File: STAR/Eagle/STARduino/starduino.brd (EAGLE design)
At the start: 101.6 x 38.1 mm, 80 parts, among them J3 J30J-15J30, J4 J30J-31J30, Q2 BSS8402DW, Q3 BSS8402DW, U1 SSCMNNN015PA2A3, U10 MC14504BDTG, U11 MAX31725MTA+, U12 TCA9535_RTW_24, U13 BMX055, U15 MC74VHC1GT125, U16 PCA9515A, U17 PCA9306DCT, U18 LT8616, U4 DS3231MZ+, U6 ATSAMD21G18, U8 ADXL375BCCZ

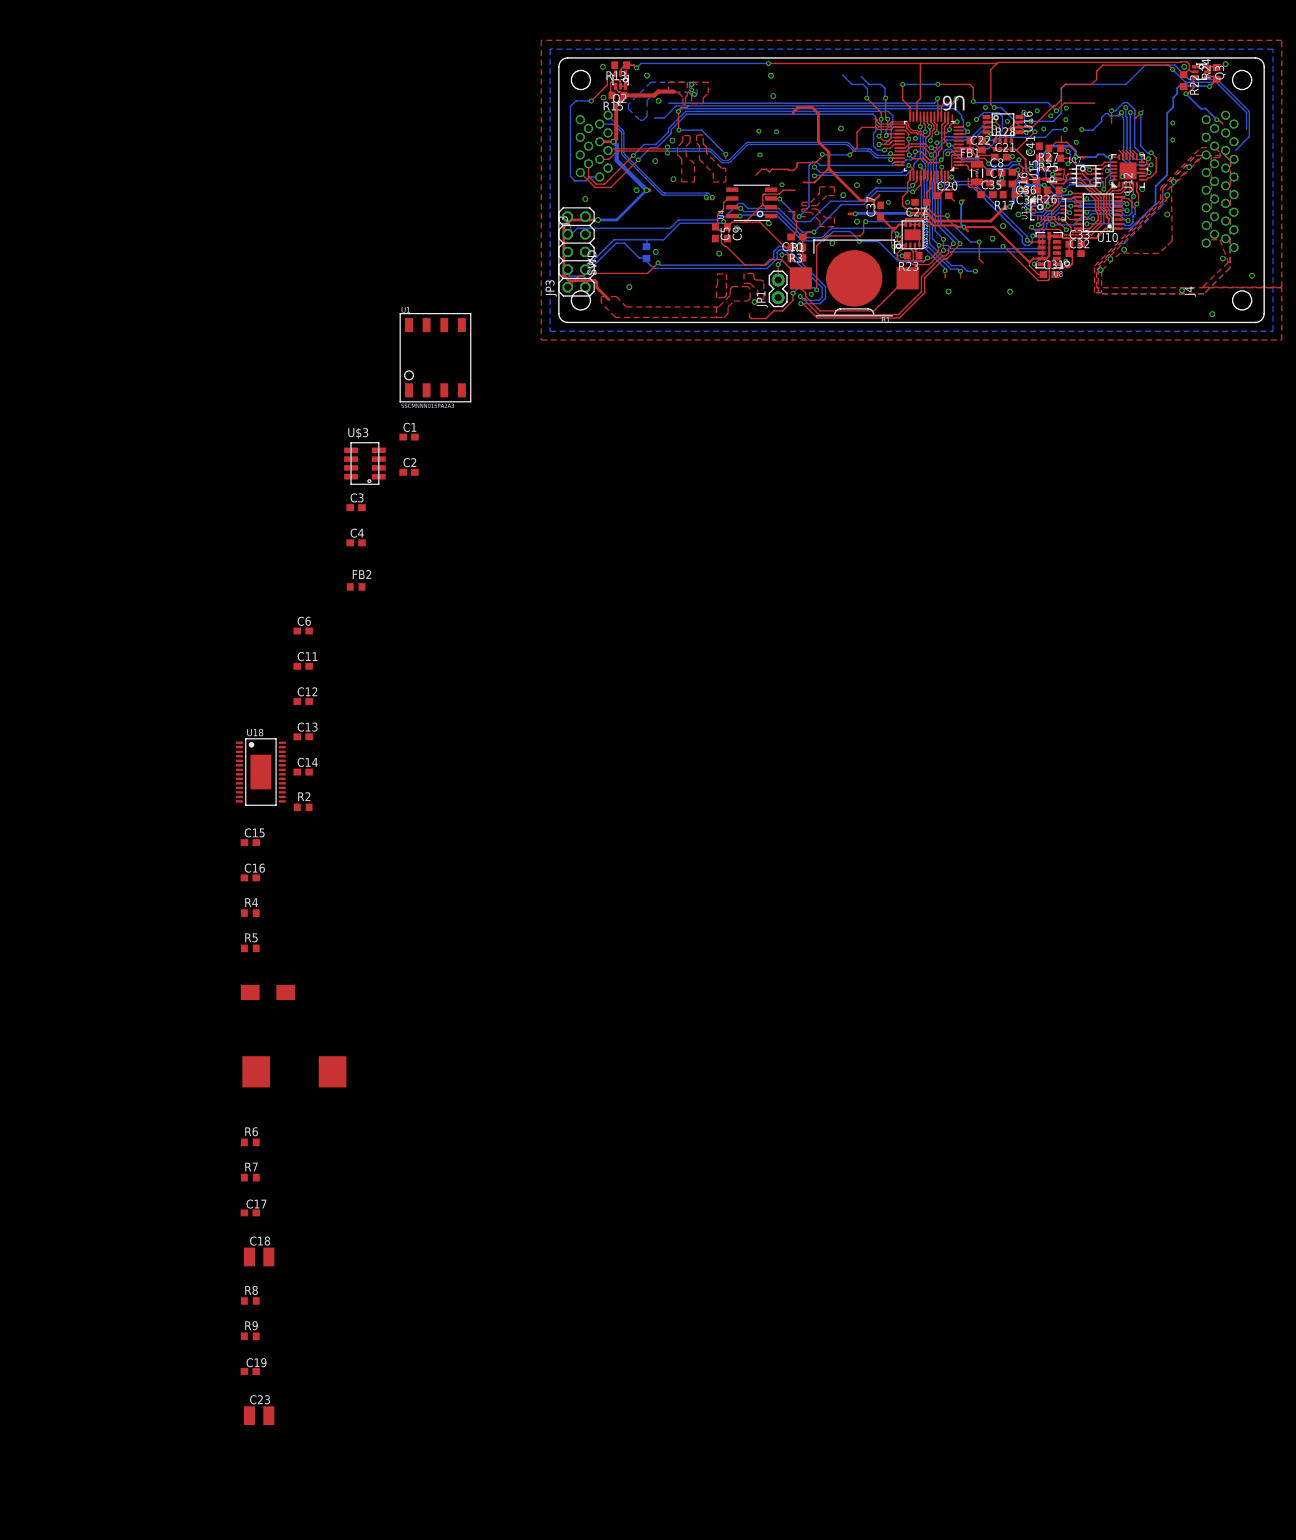
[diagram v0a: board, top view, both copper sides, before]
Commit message: datalogger differential pairs
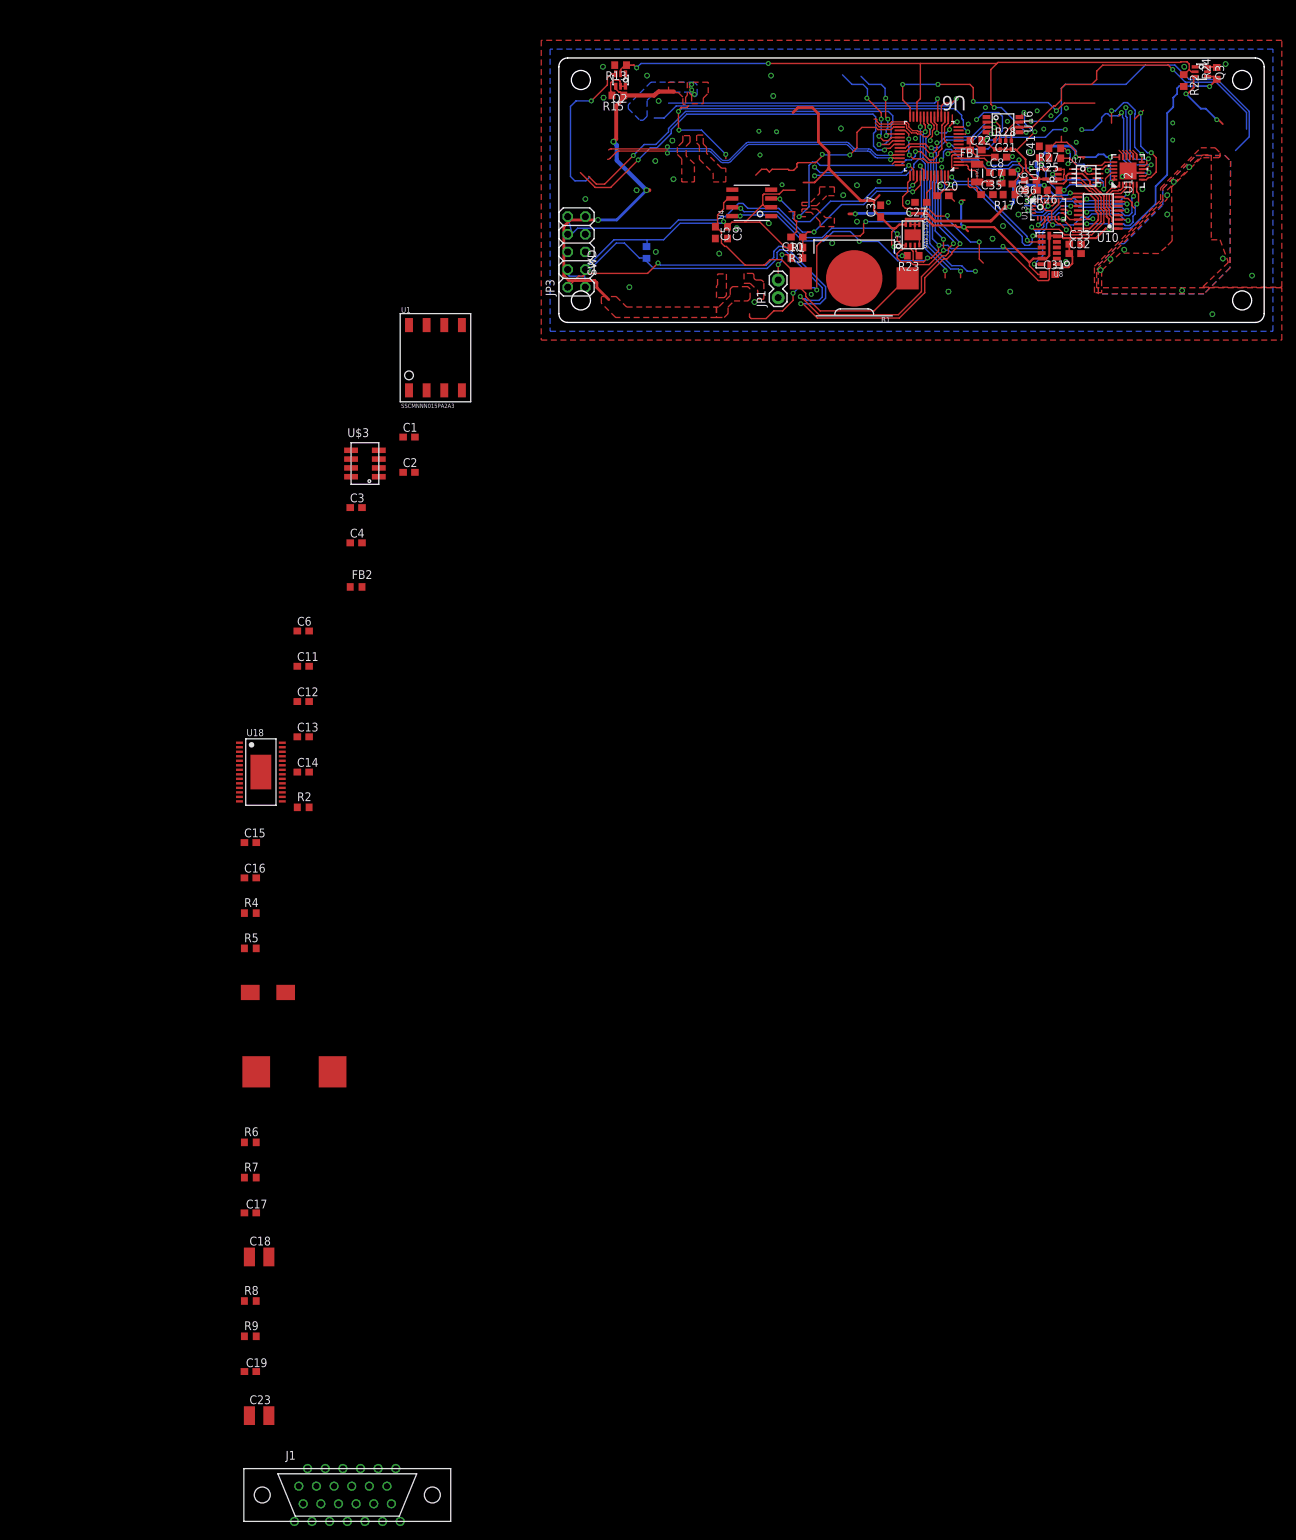
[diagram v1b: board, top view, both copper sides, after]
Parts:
- removed J3: J30J-15J30, CM_J30J:ZKN-15-J30
- removed J4: J30J-31J30, CM_J30J:ZKN-31-J30
- added J1: J30J-25, CM_J30J:ZKN-25
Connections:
- removed net PI_D_N: J3.7
- removed net PI_D_P: J3.8
- new net BIAS_REF: J1.2, U6.7
- new net D: J1.10
- new net N$27: J1.11
- new net N$32: J1.12
- new net N$36: J1.13
- new net SD_STAR: J1.9
- net +3V3: now also J1.14
- net +5V: now also J1.15, J1.16, J1.17, J1.18, J1.19; no longer J3.5
- net DEBUG_5V: no longer J3.1
- net GND: now also J1.20, J1.21, J1.22, J1.23, J1.24, J1.25; no longer J3.14, J3.2, J3.6
- net MISO: now also J1.3, J1.4
- net MOSI: now also J1.5, J1.6
- net RX2: no longer J3.9
- net SCK: now also J1.7, J1.8
- net TX2: no longer J3.10
- net USB_D_N: no longer J3.4
- net USB_D_P: no longer J3.3
- net VDD: now also J1.1
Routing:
- net PI_D_N: track 22.9 -> 0.00 mm, vias 1 -> 0
- net PI_D_P: track 22.8 -> 0.00 mm, vias 1 -> 0
- net +5V: track 57.4 -> 55.5 mm
- net TX2: track 59.6 -> 57.8 mm
- net DEBUG_5V: track 23.9 -> 22.4 mm
- net USB_D_P: track 47.0 -> 45.9 mm

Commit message: got rid of old STARduino routing
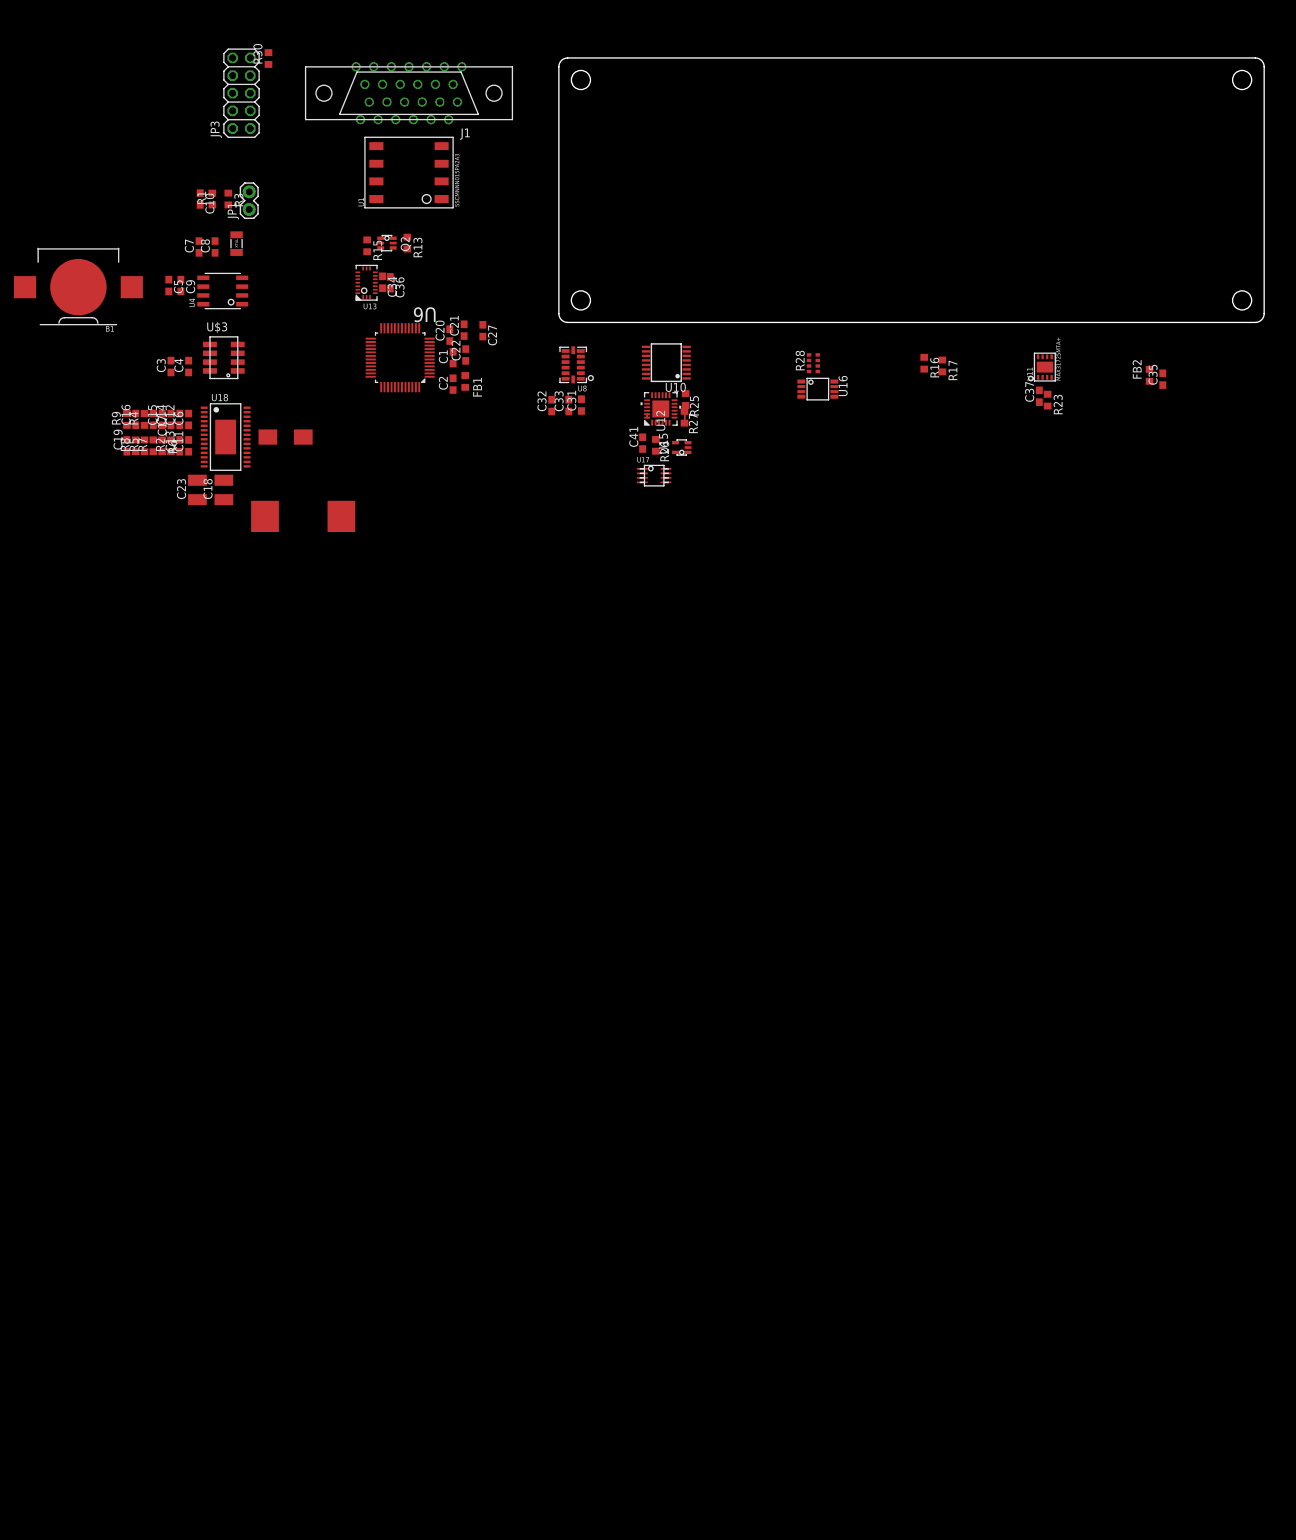
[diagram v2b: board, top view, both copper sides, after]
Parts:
- removed Q3: BSS8402DW, transistor-fet:SC70
- removed R22: 100k, resistor:R0603
- removed R24: 191k, resistor:R0603
- moved J1 202.1 mm to (-21.6, 33.0), turned to 180 degrees
- moved C19 134.5 mm to (-62.2, -17.8), turned to 90 degrees
- moved C23 133.6 mm to (-52.1, -24.1), turned to 90 degrees
- moved R9 133.3 mm to (-62.2, -14.0), turned to 90 degrees
- moved R8 124.3 mm to (-61.0, -17.8), turned to 90 degrees
- moved FB2 118.3 mm to (85.1, -7.62), turned to 90 degrees
- moved C17 115.2 mm to (-58.4, -14.0), turned to 270 degrees
- moved C7 115.1 mm to (-51.8, 10.9), turned to 90 degrees
- moved C8 113.0 mm to (-49.5, 10.9), turned to 90 degrees
- moved B1 111.8 mm to (-69.2, 5.08)
- moved C18 110.6 mm to (-48.3, -24.1), turned to 90 degrees
- moved XTAL1 107.2 mm to (-46.4, 11.4)
- moved R7 106.3 mm to (-58.4, -17.8), turned to 90 degrees
- moved R6 101.1 mm to (-57.1, -17.8), turned to 270 degrees
- moved U13 98.8 mm to (-27.7, 5.71), turned to 180 degrees
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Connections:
- removed net EXTERNAL_3V3: Q3.3
- removed net N$18: Q3.5, Q3.6, R24.2
- new net N$2: C4.2, U$3.P$5
- net +3V3: no longer Q3.4, R24.1
- net EXTERNAL_KILL: no longer Q3.2, R22.1
- net GND: no longer C4.2, Q3.1, R22.2, U$3.P$5
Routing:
- net +3V3: track 250.0 -> 0.00 mm, vias 15 -> 0
- net SCL: track 132.8 -> 0.00 mm, vias 10 -> 0
- net SDA: track 113.8 -> 0.00 mm, vias 8 -> 0
- net EXTERNAL_KILL: track 108.1 -> 0.00 mm, vias 4 -> 0
- net SWDIO: track 91.8 -> 0.00 mm, vias 4 -> 0
- net SWDCLK: track 91.0 -> 0.00 mm, vias 3 -> 0
- net 5V_S: track 85.4 -> 3.05 mm, vias 10 -> 0
- net RESET: track 65.5 -> 0.00 mm, vias 2 -> 0
- net I_SENSE: track 59.0 -> 0.00 mm, vias 4 -> 0
- net TX2: track 57.8 -> 0.00 mm, vias 2 -> 0
- net RX2: track 57.0 -> 0.00 mm, vias 2 -> 0
- net +5V: track 55.5 -> 0.00 mm, vias 3 -> 0
- net SCL_BUFF: track 51.7 -> 0.00 mm, vias 1 -> 0
- net TX0: track 48.9 -> 0.00 mm, vias 1 -> 0
- net SDA_BUFF: track 46.2 -> 0.00 mm, vias 1 -> 0
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- removed copper zone on layer 1, net +5V
- removed copper zone on layer 1, net 5V_S
- removed copper zone on layer 1, net GND
- removed copper zone on layer 16, net GND
- removed copper zone on layer 1, net N$15
- removed copper zone on layer 1, net N$39
- removed copper zone on layer 1, net N$40
- removed copper zone on layer 1, net N$50
- removed copper zone on layer 1, net N$51
- removed copper zone on layer 1, net VCC
- removed copper zone on layer 16, net VCC
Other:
- board text added: "STARduino"
- board text removed: "5-2017 Rev. 2"
- board text removed: "SWD"

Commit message: half a routed STARduino
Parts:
- moved B1 112.2 mm to (39.7, 32.1), turned to 0 degrees
- moved C23 98.1 mm to (39.1, 12.1), turned to 180 degrees
- moved R6 95.2 mm to (20.7, 37.0), turned to 180 degrees
- moved R7 94.0 mm to (18.5, 36.3)
- moved R4 93.8 mm to (20.6, 34.6), turned to 0 degrees
- moved C17 93.4 mm to (20.6, 35.8), turned to 180 degrees
- moved C16 92.6 mm to (21.0, 29.1), turned to 180 degrees
- moved R5 89.7 mm to (18.0, 27.0), turned to 180 degrees
- moved C15 89.7 mm to (19.9, 31.9)
- moved C13 87.0 mm to (18.5, 29.5), turned to 270 degrees
- moved C19 86.4 mm to (12.3, 26.0)
- moved C5 84.6 mm to (25.0, 29.2), turned to 180 degrees
- moved R8 83.0 mm to (9.53, 26.0)
- moved L1 82.8 mm to (26.1, 34.2)
- moved C11 81.5 mm to (7.75, 36.1), turned to 270 degrees
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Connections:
- removed net N$13: C15.2
- removed net N$16: C16.2
- net GND: now also C3.1
- net N$14: now also C15.2
- net N$17: now also C16.2
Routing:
- net +3V3: track 0.00 -> 194.8 mm, vias 0 -> 2
- net +5V: track 0.00 -> 89.4 mm, vias 0 -> 2
- net GND: track 0.00 -> 43.6 mm, vias 0 -> 5
- net N$8: track 0.00 -> 34.0 mm, vias 0 -> 2
- net RESET: track 0.00 -> 24.9 mm, vias 0 -> 2
- net VDD: track 0.00 -> 22.3 mm, vias 0 -> 2
- net N$37: track 0.00 -> 16.4 mm, vias 0 -> 2
- net N$1: track 0.00 -> 15.4 mm, vias 0 -> 2
- net SCL: track 0.00 -> 12.0 mm, vias 0 -> 2
- net SDA: track 0.00 -> 11.7 mm, vias 0 -> 2
- net N$21: track 0.00 -> 10.8 mm, vias 0 -> 2
- net N$11: track 0.00 -> 10.8 mm, vias 0 -> 2
- net SDA_BUFF: track 0.00 -> 10.7 mm
- net N$6: track 0.00 -> 10.6 mm, vias 0 -> 2
- net SCL_BUFF: track 0.00 -> 9.46 mm
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- added copper zone on layer 1, net GND
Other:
- board size 101.6 x 38.1 mm -> 59.8 x 38.2 mm

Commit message: STARduino
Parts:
- moved U$1 39.9 mm to (25.2, 12.1)
- moved U$2 39.9 mm to (12.3, 11.9)
- moved C27 2.53 mm to (21.4, 17.3), turned to 90 degrees
- moved XTAL1 2.12 mm to (22.7, 11.1)
- moved C7 1.82 mm to (25.3, 12.4), turned to 180 degrees
- moved C18 1.79 mm to (19.4, 11.0)
- moved C23 1.53 mm to (39.0, 10.6)
- moved U12 1.14 mm to (45.4, 23.0)
- moved C8 0.48 mm to (27.9, 9.45), turned to 270 degrees
- moved C41 0.32 mm to (47.7, 9.40)
- moved FB2 0.09 mm to (51.1, 2.22)
- moved C33 0.06 mm to (53.8, 2.24)
- moved C35 0.06 mm to (52.5, 2.24)
- moved C11 0.06 mm to (7.75, 36.2)
- moved C31 0.06 mm to (52.5, 5.30)
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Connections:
- net +3V3: now also J1.1, J1.3; no longer J1.14
- net +5V: now also J1.20, J1.5, J1.6, J1.8; no longer J1.15, J1.16, J1.17, J1.18
- net GND: now also J1.7; no longer J1.20, J1.25
- net MISO: now also J1.15, J1.17; no longer J1.3, J1.4
- net MOSI: now also J1.14, J1.4; no longer J1.5, J1.6
- net SCK: now also J1.16, J1.18; no longer J1.7, J1.8
- net VDD: now also J1.25; no longer J1.1
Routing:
- net GND: track 43.6 -> 238.4 mm, vias 5 -> 30
- net SCL: track 12.0 -> 99.6 mm, vias 2 -> 8
- net SDA: track 11.7 -> 97.1 mm, vias 2 -> 8
- net +3V3: track 194.8 -> 251.6 mm, vias 2 -> 7
- net VDD: track 22.3 -> 74.6 mm, vias 2 -> 3
- net 5V_S: track 1.92 -> 49.6 mm, vias 0 -> 2
- net SCK: track 0.00 -> 47.3 mm, vias 0 -> 1
- net MOSI: track 0.00 -> 46.5 mm, vias 0 -> 1
- net VREFA: track 1.34 -> 43.6 mm, vias 0 -> 4
- net MISO: track 0.00 -> 41.8 mm, vias 0 -> 1
- net BIAS_REF: track 0.00 -> 37.6 mm, vias 0 -> 1
- net IMUINT5: track 0.00 -> 32.0 mm, vias 0 -> 2
- net V_SENSE: track 0.00 -> 31.7 mm, vias 0 -> 2
- net SWDIO: track 0.00 -> 31.2 mm, vias 0 -> 4
- net IMUDR: track 0.00 -> 30.2 mm, vias 0 -> 2
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- removed copper zone on layer 1, net GND
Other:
- board size 59.8 x 38.2 mm -> 59.7 x 38.2 mm
- board text added: "2018STARduino Rev. 1"
- board text removed: "STARduino"

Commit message: misc board stuff
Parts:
- moved C37 0.57 mm to (49.9, 5.87)
- moved R16 0.57 mm to (47.0, 6.00)
- moved R17 0.57 mm to (48.5, 5.92)
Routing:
- net GND: track 238.4 -> 256.4 mm, vias 30 -> 41
- net EXTERNAL_KILL: track 34.5 -> 38.1 mm
- net +3V3: track 251.6 -> 252.3 mm
- net 5V_S: track 49.6 -> 49.0 mm
- added copper zone on layer 1, net GND
- added copper zone on layer 16, net GND
